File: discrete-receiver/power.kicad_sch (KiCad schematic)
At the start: 32 parts, among them J2 Optional 5V DC Jack, U11 Ag9905LP, U12 TPS7A20xxxDBV, U13 LM66100DCK, U14 LM66100DCK, U15 LM66100DCK, U8 AMS1117

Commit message: Progress on power design
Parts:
- removed FB3: FB, symbol Device:FerriteBead_Small
- added C71: 100nF, PCM_JLCPCB:C_0402, symbol PCM_JLCPCB-Capacitors:0402,100nF
- added R10: 10kΩ, PCM_JLCPCB:R_0402, symbol PCM_JLCPCB-Resistors:0402,10kΩ
- added R3: 49.9kΩ, PCM_JLCPCB:R_0402, symbol PCM_JLCPCB-Resistors:0402,49.9kΩ
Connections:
- net +5V: now also U20.5 (EN), U20.7 (IN), U20.8 (IN)
- net +5V_A: now also U20.1 (OUT), U20.2 (OUT), R3.2
- net GND: now also U20.4 (GND), U20.9 (EP), C71.1, R10.2
- net at U20.3 (FB): now also R10.1, R3.1
- net at U20.6 (NR): now also C71.2
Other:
- moved on the sheet: C32, C33, C34, TP13, TP7, U12, U20

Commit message: Power page draft complete
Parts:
- removed C70: 100pF, PCM_JLCPCB:C_0603, symbol PCM_JLCPCB-Capacitors:0603,100pF
- removed JP7, JP8: SolderJumper_Bridged, symbol Jumper:SolderJumper_2_Bridged
- removed U12: TPS7A20xxxDBV, Package_TO_SOT_SMD:SOT-23-5, symbol Regulator_Linear:TPS7A20xxxDBV
- removed U8: AMS1117, PCM_JLCPCB:SOT-223-3_L6.5-W3.4-P2.30-LS7.0-BR, symbol PCM_JLCPCB-Power:LDO, 3.3V, 1A
- added C70, C72, C74, C92: 100nF, PCM_JLCPCB:C_0402, symbol PCM_JLCPCB-Capacitors:0402,100nF
- added C73, C76, C77, C78, C90, C93, C94: 100pF, PCM_JLCPCB:C_0603, symbol PCM_JLCPCB-Capacitors:0603,100pF
- added C75, C91: 10uF, PCM_JLCPCB:C_0603, symbol PCM_JLCPCB-Capacitors:0603,10uF,(2)
- added R27: 20kΩ, PCM_JLCPCB:R_0402, symbol PCM_JLCPCB-Resistors:0402,20kΩ
- added R35: 10kΩ, PCM_JLCPCB:R_0402, symbol PCM_JLCPCB-Resistors:0402,10kΩ
- added TP14: +2.4V_A, symbol Connector:TestPoint
- added TP15: +3.3V_A, symbol Connector:TestPoint
- added U12, U8: (no value), EasyEDA_Lib:SOT-223-3_L6.5-W3.4-P2.30-LS7.0-BR, symbol EasyEDA_Lib:SGM2212-3.3XKC3G/TR_C3294699
- added U21: (no value), EasyEDA_Lib:TDFN-8_L3.0-W3.0-P0.65-BL-EP2.3, symbol EasyEDA_Lib:HX59800-SQ
- TP13: value VDDA -> +4.8V_A
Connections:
- net +3.3V: now also C70.1, C94.1, U8.2 (VOUT), U8.4 (VOUT)
- net +3.3V_A: now also C91.1, C92.1, C93.1, TP15.1, U12.2 (VOUT), U12.4 (VOUT)
- net +5V: now also C76.2, C77.2, C78.2, C90.2, U12.3 (VIN), U21.5 (EN), U21.7 (IN), U21.8 (IN), U8.3 (VIN)
- net GND: now also C70.2, C72.1, C73.2, C74.2, C75.2, C76.1, C77.1, C78.1, C90.1, C91.2, C92.2, C93.2, C94.2, R35.2, U12.1 (GND), U21.4 (GND), U21.9 (EP), U8.1 (GND)
- net +5V_A renamed +4.8V_A
- new net: R27.2, R35.1, U21.3 (FB)
- new net: C72.2, U21.6 (NR)
- new net +2.4V_A: C73.1, C74.1, C75.1, R27.1, TP14.1, U21.1 (OUT), U21.2 (OUT)
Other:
- note added: "+2.4V Regulator"
- note added: "+4.8V Regulator"
- note added: "3.3V Regulator"
- note added: "3.3V_A Regulator"
- note removed: "3.3V LDO Regulator"
- note removed: "Old Voltage Regulator"
- moved on the sheet: C55, C60, D3, D4, JP1, TP10, U11

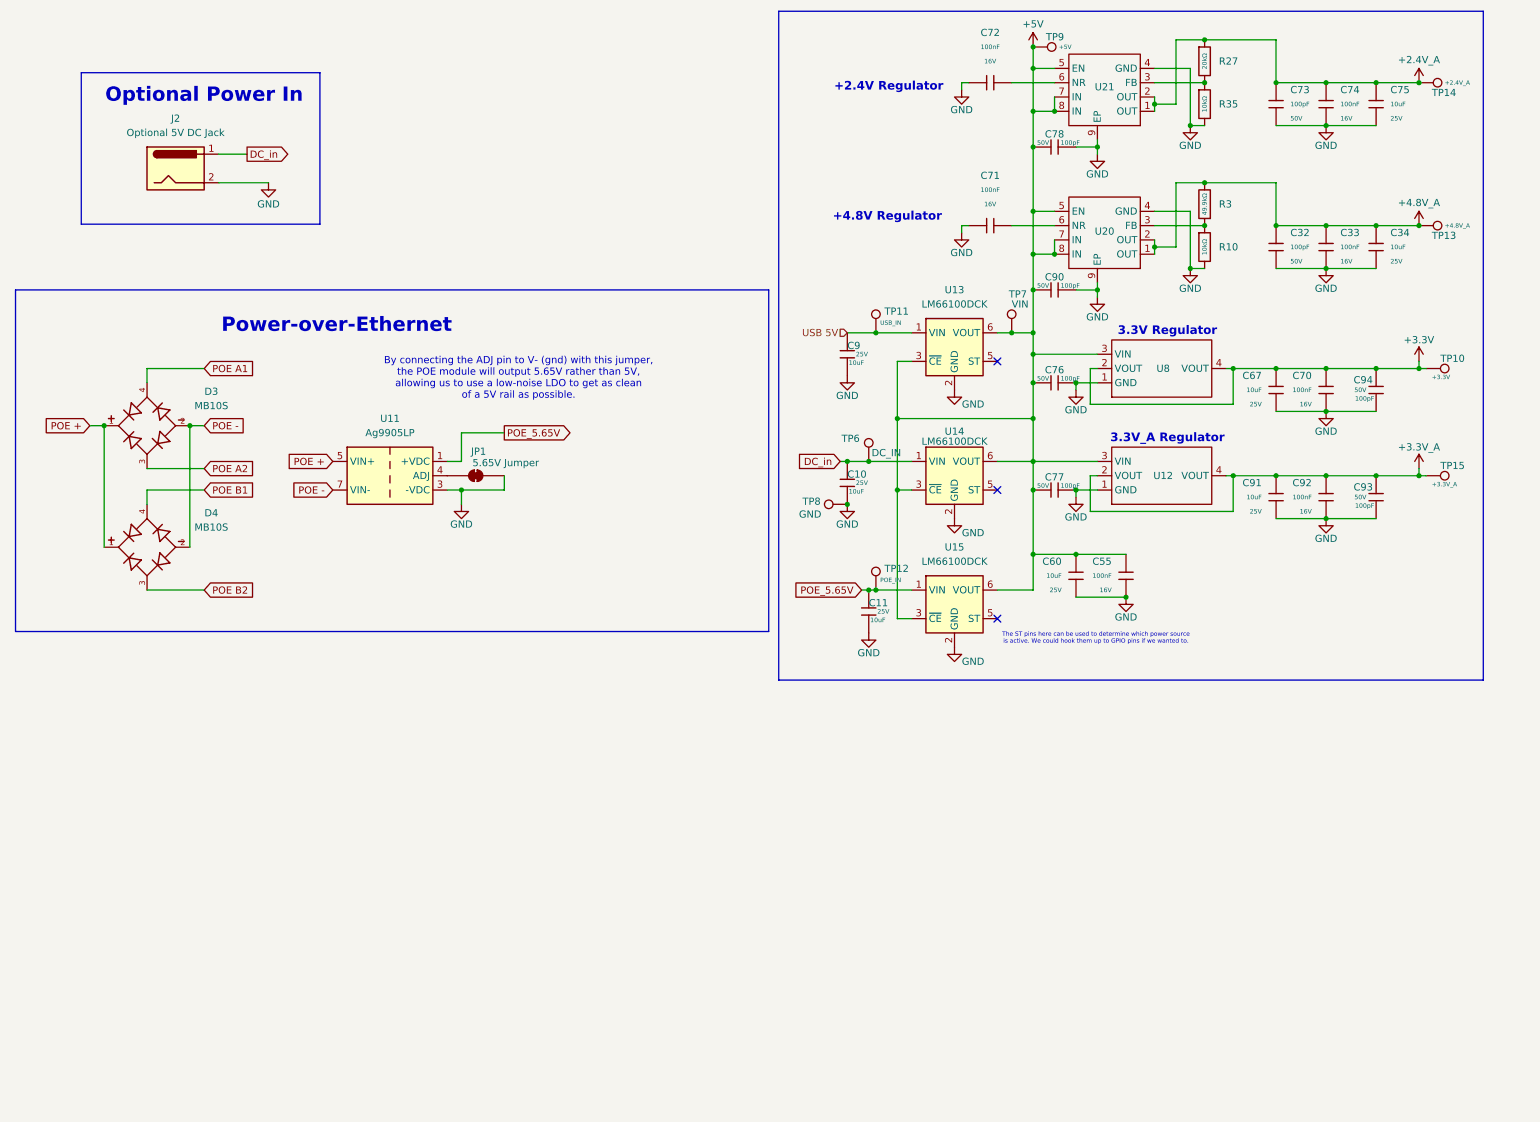
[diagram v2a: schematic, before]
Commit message: Redone draft of power page
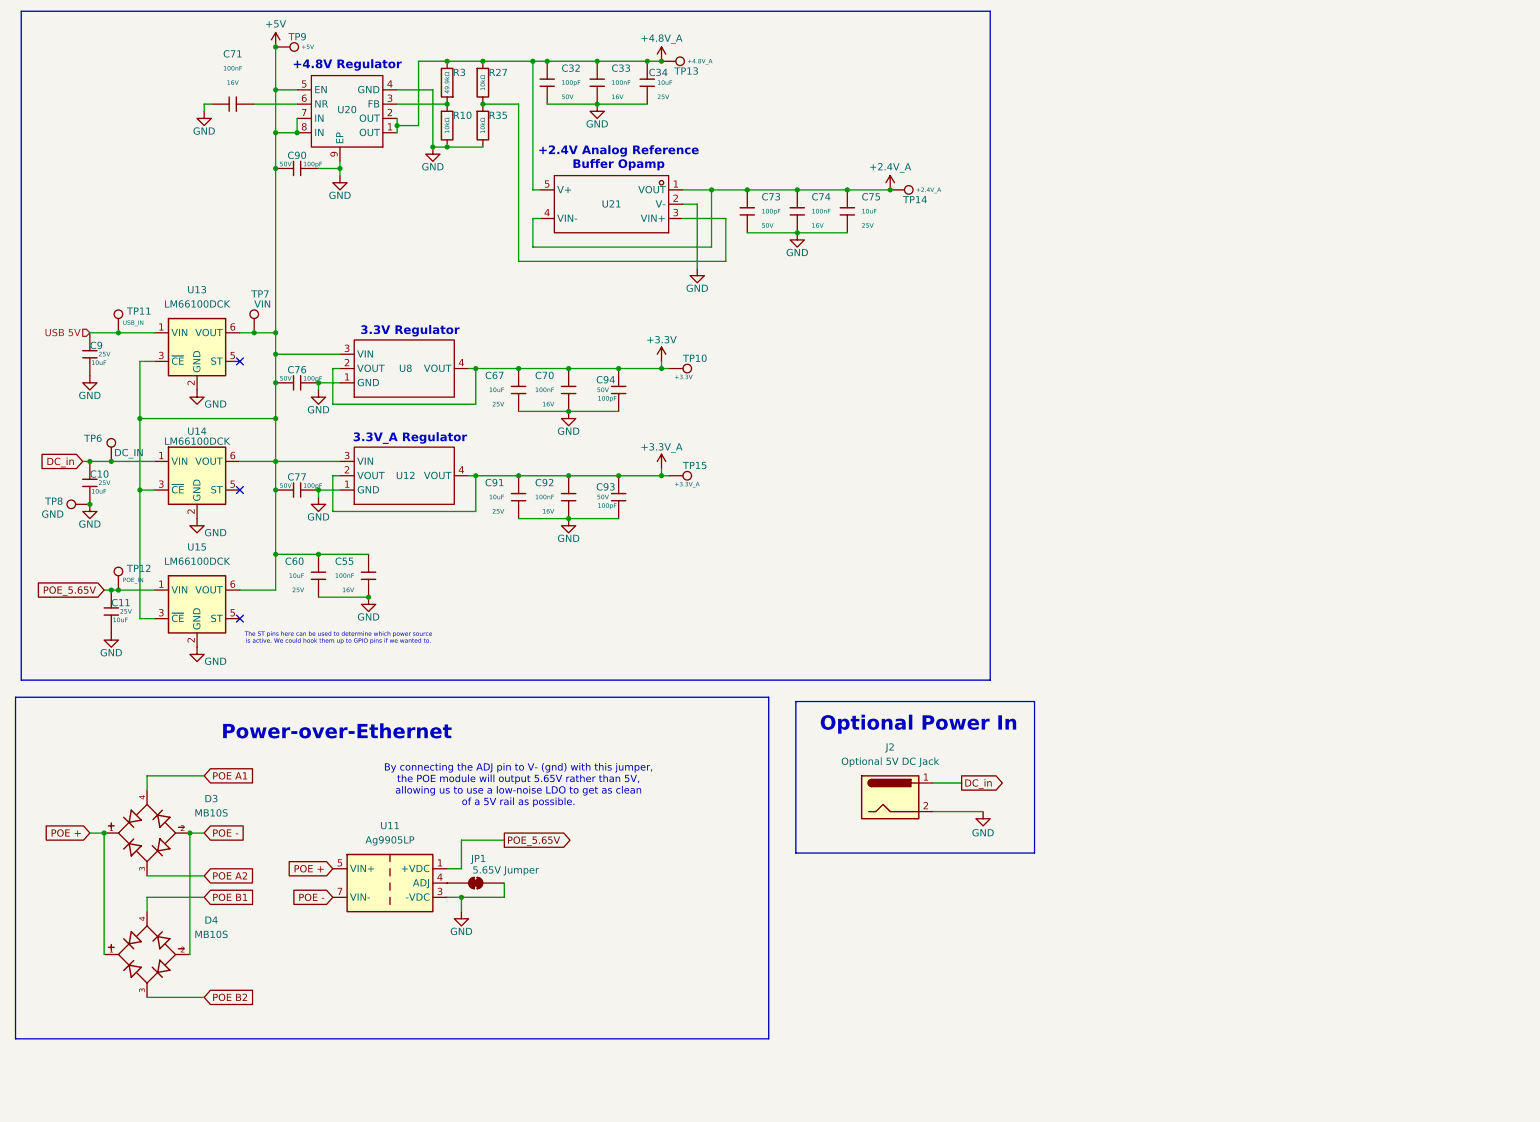
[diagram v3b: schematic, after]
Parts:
- removed C72: 100nF, PCM_JLCPCB:C_0402, symbol PCM_JLCPCB-Capacitors:0402,100nF
- removed C78: 100pF, PCM_JLCPCB:C_0603, symbol PCM_JLCPCB-Capacitors:0603,100pF
- removed R27: 20kΩ, PCM_JLCPCB:R_0402, symbol PCM_JLCPCB-Resistors:0402,20kΩ
- removed U21: (no value), EasyEDA_Lib:TDFN-8_L3.0-W3.0-P0.65-BL-EP2.3, symbol EasyEDA_Lib:HX59800-SQ
- added R27: 10kΩ, PCM_JLCPCB:R_0402, symbol PCM_JLCPCB-Resistors:0402,10kΩ
- added U21: (no value), EasyEDA_Lib:SOT-23-5_L3.0-W1.7-P0.95-LS2.8-BL, symbol EasyEDA_Lib:RS8551XF
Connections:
- net +2.4V_A: now also U21.1 (VOUT), U21.4 (VIN-)
- net +4.8V_A: now also R27.1, U21.5 (V+)
- net GND: now also U21.2 (V-)
- net at R35.1: now also R27.2, U21.3 (VIN+)
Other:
- note added: "+2.4V Analog Reference Buffer Opamp"
- note removed: "+2.4V Regulator"
- moved on the sheet: C10, C11, C32, C33, C34, C55, C60, C67, C70, C71, C73, C74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

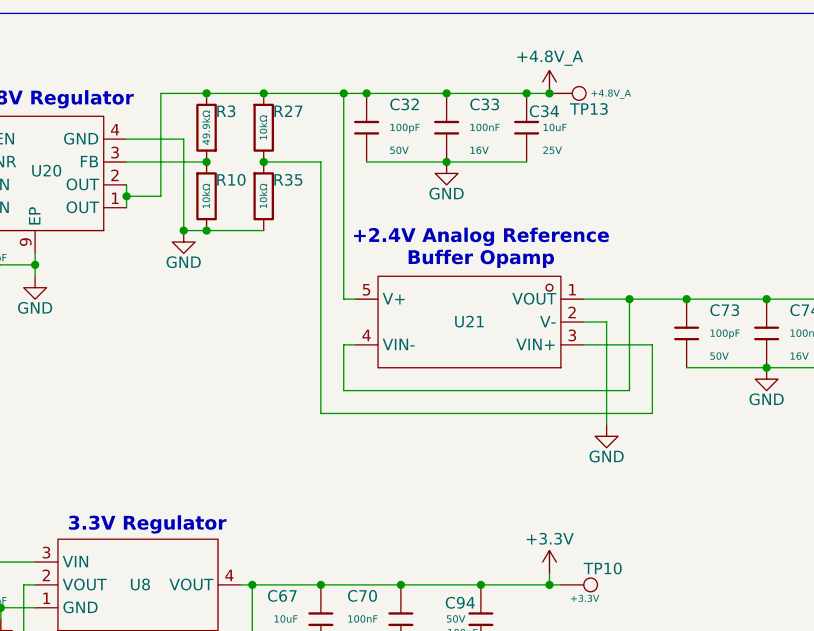
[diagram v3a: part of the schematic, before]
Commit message: Power page updates
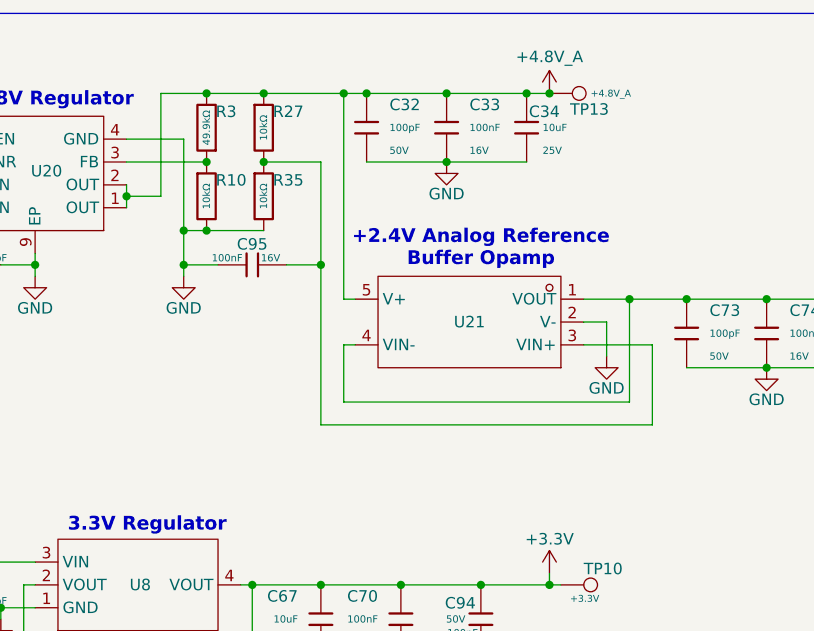
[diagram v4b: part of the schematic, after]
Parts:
- added C95: 100nF, PCM_JLCPCB:C_0402, symbol PCM_JLCPCB-Capacitors:0402,100nF
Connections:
- net GND: now also C95.1
- net at R27.2, R35.1, U21.3 (VIN+): now also C95.2

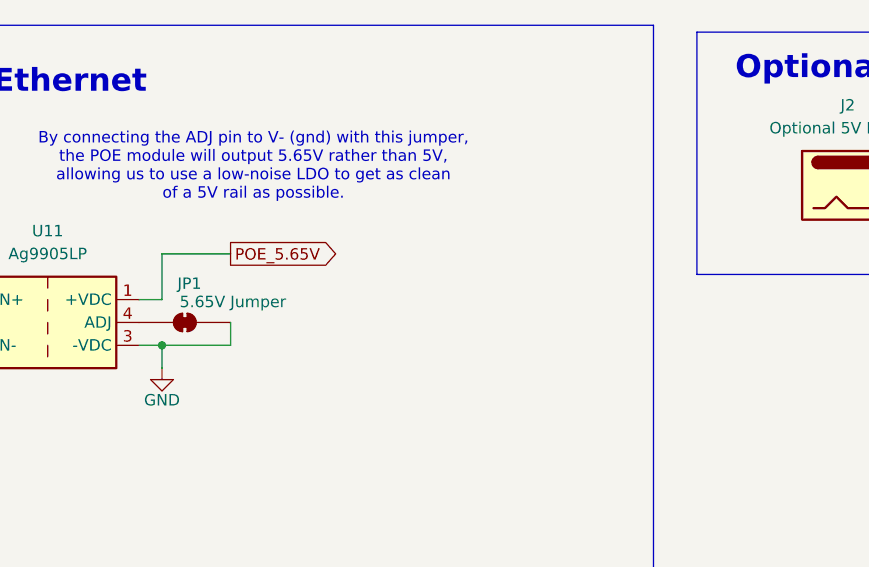
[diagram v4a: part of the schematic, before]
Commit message: Added note on PoE output filter
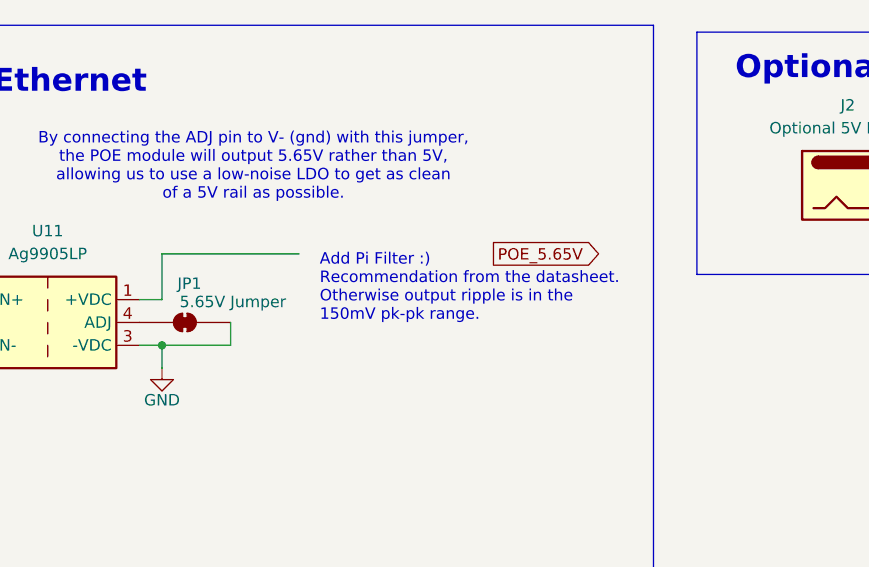
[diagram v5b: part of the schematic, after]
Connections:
- net POE_5.65V: no longer U11.1 (+VDC), U11.2 (+VDC)
- new net: U11.1 (+VDC), U11.2 (+VDC)
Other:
- note added: "Add Pi Filter :) Recommendation from the datasheet. Otherwise output ripple is in the 150mV pk-pk range."
